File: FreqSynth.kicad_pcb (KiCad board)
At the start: 4 copper layers, 49 x 50 mm, 841 parts, among them P1 CPL-CON-BARREL-2.1MM, P2 RF1, P3 RF2, P4 CONN_01X03, P5 REF_IN, P6 SWD, U1 MAX2870, U10 PE43711, U11 LMH2110, U12 STM32F030K6T6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

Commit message: RC1
Signed-off-by: Martin Berglund <LeastSignificantBit@users.noreply.github.com>
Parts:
- added ?: , FreqSynth:VIA, F.Cu at (127.0, 135.0)
- added ?: , FreqSynth:VIA, F.Cu at (127.0, 137.4)
- added ?: , FreqSynth:VIA, F.Cu at (121.8, 141.5)
- added ?: , FreqSynth:VIA, F.Cu at (123.8, 141.5)
- added ?: , FreqSynth:VIA, F.Cu at (123.0, 140.4)
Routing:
- net Earth: track 143.1 -> 143.9 mm
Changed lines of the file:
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@@
 (kicad_pcb (version 20160815) (host pcbnew 4.X.X-debug)
   (general
-    (links 0)
+    (links 1032)
     (no_connects 0)
     (area 100.424999 99.924999 149.575001 150.075001)
     (thickness 1.6)
     (drawings 59)
-    (tracks 949)
+    (tracks 952)
     (zones 0)
-    (modules 841)
+    (modules 846)
     (nets 103)
   )
@@
   )
   (setup
-    (last_trace_width 0.1905)
+    (last_trace_width 0.127)
     (user_trace_width 0.1905)
     (user_trace_width 0.254)
@@
     (pad_drill 0.254)
     (pad_to_mask_clearance 0.05)
-    (pad_to_paste_clearance -0.1)
+    (pad_to_paste_clearance -0.05)
     (aux_axis_origin 0 0)
     (visible_elements FFFFFF7F)
@@
   )
   (module FreqSynth:VIA (layer F.Cu)
+    (at 127 135 90)
+    (fp_text reference "" (at 0 0.5 90) (layer F.SilkS) hide
+      (effects (font (size 0.4 0.4) (thickness 0.1)))
+    )
+    (fp_text value "" (at 0 -0.5 90) (layer F.Fab) hide
+      (effects (font (size 1 1) (thickness 0.15)))
+    )
+    (pad 1 thru_hole circle (at 0 0 90) (size 0.4572 0.4572) (drill 0.254) (layers *.Cu)
+      (net 7 Earth))
+  )
+  (module FreqSynth:VIA (layer F.Cu)
+    (at 127 137.4 90)
+    (fp_text reference "" (at 0 0.5 90) (layer F.SilkS) hide
+      (effects (font (size 0.4 0.4) (thickness 0.1)))
+    )
+    (fp_text value "" (at 0 -0.5 90) (layer F.Fab) hide
+      (effects (font (size 1 1) (thickness 0.15)))
+    )
+    (pad 1 thru_hole circle (at 0 0 90) (size 0.4572 0.4572) (drill 0.254) (layers *.Cu)
+      (net 7 Earth))
+  )
+  (module FreqSynth:VIA (layer F.Cu)
+    (at 121.75 141.5 90)
+    (fp_text reference "" (at 0 0.5 90) (layer F.SilkS) hide
+      (effects (font (size 0.4 0.4) (thickness 0.1)))
+    )
+    (fp_text value "" (at 0 -0.5 90) (layer F.Fab) hide
+      (effects (font (size 1 1) (thickness 0.15)))
+    )
+    (pad 1 thru_hole circle (at 0 0 90) (size 0.4572 0.4572) (drill 0.254) (layers *.Cu)
+      (net 7 Earth))
+  )
+  (module FreqSynth:VIA (layer F.Cu)
+    (at 123.75 141.5 90)
+    (fp_text reference "" (at 0 0.5 90) (layer F.SilkS) hide
+      (effects (font (size 0.4 0.4) (thickness 0.1)))
+    )
+    (fp_text value "" (at 0 -0.5 90) (layer F.Fab) hide
+      (effects (font (size 1 1) (thickness 0.15)))
+    )
+    (pad 1 thru_hole circle (at 0 0 90) (size 0.4572 0.4572) (drill 0.254) (layers *.Cu)
+      (net 7 Earth))
+  )
+  (module FreqSynth:VIA (layer F.Cu)
+    (at 123 140.4 90)
+    (fp_text reference "" (at 0 0.5 90) (layer F.SilkS) hide
+      (effects (font (size 0.4 0.4) (thickness 0.1)))
+    )
+    (fp_text value "" (at 0 -0.5 90) (layer F.Fab) hide
+      (effects (font (size 1 1) (thickness 0.15)))
+    )
+    (pad 1 thru_hole circle (at 0 0 90) (size 0.4572 0.4572) (drill 0.254) (layers *.Cu)
+      (net 7 Earth))
+  )
+  (module FreqSynth:VIA (layer F.Cu)
     (at 142.45 130.85)
     (fp_text reference "" (at 0 0.5) (layer F.SilkS) hide
@@
     (tags "resistor 0603")
     (attr smd)
-    (fp_text reference R2 (at 0 -1.25 360) (layer F.SilkS)
+    (fp_text reference R2 (at 0 -1.25) (layer F.SilkS)
       (effects (font (size 0.4 0.4) (thickness 0.1)))
     )
@@
     (tags "capacitor 0402")
     (attr smd)
-    (fp_text reference C21 (at -0.05104 1.237437 360) (layer F.SilkS)
+    (fp_text reference C21 (at -0.05104 1.237437) (layer F.SilkS)
       (effects (font (size 0.4 0.4) (thickness 0.1)))
     )
@@
     (tags "capacitor 0402")
     (attr smd)
-    (fp_text reference C9 (at -0.9 -1.35 360) (layer F.SilkS)
+    (fp_text reference C9 (at -0.9 -1.35) (layer F.SilkS)
       (effects (font (size 0.4 0.4) (thickness 0.1)))
     )
@@
     (tags "capacitor 0402")
     (attr smd)
-    (fp_text reference C10 (at -0.141421 -1.202082 360) (layer F.SilkS)
+    (fp_text reference C10 (at -0.141421 -1.202082) (layer F.SilkS)
       (effects (font (size 0.4 0.4) (thickness 0.1)))
     )
@@
     (tags "resistor 0402")
     (attr smd)
-    (fp_text reference R5 (at 1.35 -0.05 360) (layer B.SilkS)
+    (fp_text reference R5 (at 1.35 -0.05) (layer B.SilkS)
       (effects (font (size 0.4 0.4) (thickness 0.1)) (justify mirror))
     )
@@
     (tags "resistor 0402")
     (attr smd)
-    (fp_text reference R9 (at 1.35 -0.05 360) (layer B.SilkS)
+    (fp_text reference R9 (at 1.35 -0.05) (layer B.SilkS)
       (effects (font (size 0.4 0.4) (thickness 0.1)) (justify mirror))
     )
@@
     (tags "resistor 0402")
     (attr smd)
-    (fp_text reference R10 (at 0.813173 0.671751 360) (layer B.SilkS)
+    (fp_text reference R10 (at 0.813173 0.671751) (layer B.SilkS)
       (effects (font (size 0.4 0.4) (thickness 0.1)) (justify mirror))
     )
@@
     (tags "resistor 0402")
     (attr smd)
-    (fp_text reference R6 (at 0.626777 -0.883883 360) (layer B.SilkS)
+    (fp_text reference R6 (at 0.626777 -0.883883) (layer B.SilkS)
       (effects (font (size 0.4 0.4) (thickness 0.1)) (justify mirror))
     )
@@
   (segment (start 132.7 133) (end 132.218198 132.518198) (width 0.254) (layer B.Cu) (net 6))
   (via (at 132.7 133) (size 0.4572) (drill 0.254) (layers F.Cu B.Cu) (net 6))
+  (segment (start 138 107.4) (end 138 107.25) (width 0.127) (layer F.Cu) (net 7))
+  (segment (start 138 107.25) (end 137.95 107.2) (width 0.127) (layer F.Cu) (net 7))
+  (segment (start 137.95 107.2) (end 137.4 107.2) (width 0.127) (layer F.Cu) (net 7))
   (segment (start 128.75 105.5) (end 128.75 106.05) (width 0.635) (layer F.Cu) (net 7))
   (segment (start 128.75 106.05) (end 127.94 106.86) (width 0.635) (layer F.Cu) (net 7))

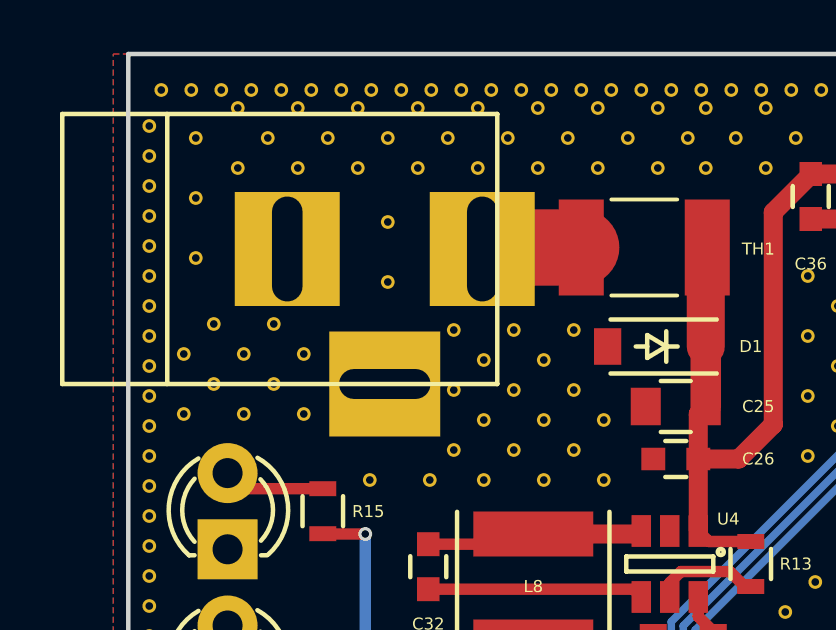
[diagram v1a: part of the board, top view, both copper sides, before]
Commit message: RC2
Fixed oval holes that are not allowed and set the solder mask parameters to the limit

Signed-off-by: Martin Berglund <LeastSignificantBit@users.noreply.github.com>
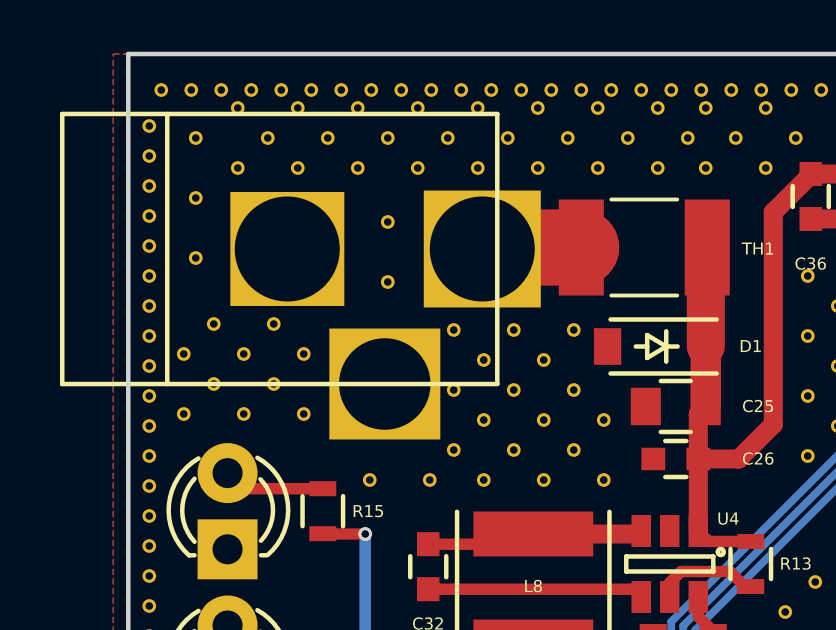
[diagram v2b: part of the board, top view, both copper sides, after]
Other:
- rule pad_to_mask_clearance: 0.05 -> 0.0635
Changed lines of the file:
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@@
 (kicad_pcb (version 20160815) (host pcbnew 4.X.X-debug)
   (general
-    (links 1032)
+    (links 1034)
     (no_connects 0)
-    (area 100.424999 99.924999 149.575001 150.075001)
+    (area 95.669289 96.924999 151.075001 153.075001)
     (thickness 1.6)
     (drawings 59)
@@
     (mod_text_size 0.4 0.4)
     (mod_text_width 0.1)
-    (pad_size 0.4572 0.4572)
-    (pad_drill 0.254)
-    (pad_to_mask_clearance 0.05)
+    (pad_size 3.8 3.8)
+    (pad_drill 3.5)
+    (pad_to_mask_clearance 0.0635)
+    (solder_mask_min_width 0.1016)
     (pad_to_paste_clearance -0.05)
     (aux_axis_origin 0 0)
     (visible_elements FFFFFF7F)
     (pcbplotparams
-      (layerselection 0x00030_ffffffff)
+      (layerselection 0x010f8_ffffffff)
       (usegerberextensions false)
       (excludeedgelayer true)
@@
       (psnegative false)
       (psa4output false)
-      (plotreference true)
-      (plotvalue true)
+      (plotreference false)
+      (plotvalue false)
       (plotinvisibletext false)
       (padsonsilk false)
@@
       (outputformat 1)
       (mirror false)
-      (drillshape 1)
+      (drillshape 0)
       (scaleselection 1)
-      (outputdirectory ""))
+      (outputdirectory Gerber/))
   )
   (net 0 "")
@@
     (fp_line (start 7.00024 4.50088) (end 7.00024 -4.50088) (layer F.SilkS) (width 0.15))
     (fp_line (start 7.00024 -4.50088) (end -7.50062 -4.50088) (layer F.SilkS) (width 0.15))
-    (pad 1 thru_hole rect (at 6.5 0) (size 3.50012 3.80012) (drill oval 1.02 3.5) (layers *.Cu *.Mask F.SilkS)
+    (pad 1 thru_hole rect (at 6.5 0) (size 3.9 3.9) (drill 3.5) (layers *.Cu *.Mask F.SilkS)
       (net 61 "Net-(P1-Pad1)"))
-    (pad 2 thru_hole rect (at 0 0) (size 3.5 3.8) (drill oval 1.02 3.5) (layers *.Cu *.Mask F.SilkS)
+    (pad 2 thru_hole rect (at 0 0) (size 3.8 3.8) (drill 3.5) (layers *.Cu *.Mask F.SilkS)
       (net 7 Earth))
-    (pad 3 thru_hole rect (at 3.25 4.5) (size 3.7 3.5) (drill oval 3.05 1) (layers *.Cu *.Mask F.SilkS)
+    (pad 3 thru_hole rect (at 3.25 4.5) (size 3.7 3.7) (drill 3.05) (layers *.Cu *.Mask F.SilkS)
       (net 7 Earth))
   )

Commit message: RC3 - fixed soldermask
Signed-off-by: Martin Berglund <LeastSignificantBit@users.noreply.github.com>
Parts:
- removed the ? at (141.9, 115.2)
- removed the ? at (141.9, 113.2)
- removed the ? at (141.9, 117.2)
- removed the ? at (142.0, 122.4)
- removed the ? at (141.0, 123.4)
- removed the ? at (141.9, 119.2)
- removed the ? at (141.9, 121.2)
- moved ? 0.25 mm to (143.0, 105.2)
- moved ? 0.25 mm to (146.0, 105.2)
- moved ? 0.25 mm to (144.0, 105.2)
- moved ? 0.25 mm to (145.0, 105.2)
- moved ? 0.25 mm to (146.0, 108.5)
- moved ? 0.25 mm to (143.0, 108.5)
- moved ? 0.25 mm to (145.0, 108.5)
- moved ? 0.25 mm to (144.0, 108.5)
- moved ? 0.25 mm to (144.2, 141.6)
- moved ? 0.25 mm to (143.2, 141.6)
- moved ? 0.25 mm to (146.2, 141.6)
- moved ? 0.25 mm to (145.2, 141.6)
- moved ? 0.25 mm to (145.2, 144.8)
- moved ? 0.25 mm to (144.2, 144.8)
- moved ? 0.25 mm to (146.2, 144.8)
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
